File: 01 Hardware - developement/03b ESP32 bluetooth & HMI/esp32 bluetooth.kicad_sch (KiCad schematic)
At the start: 48 parts, among them J1 I2C, J2 UART, J3 power supply, J4 Jtag, J5 I2S, J8 Conn_01x01_Pin, SW10 Strapping button, SW8 Strapping button, SW9 Strapping button, U2 ESP32-DevKitC, U3 MCP23008

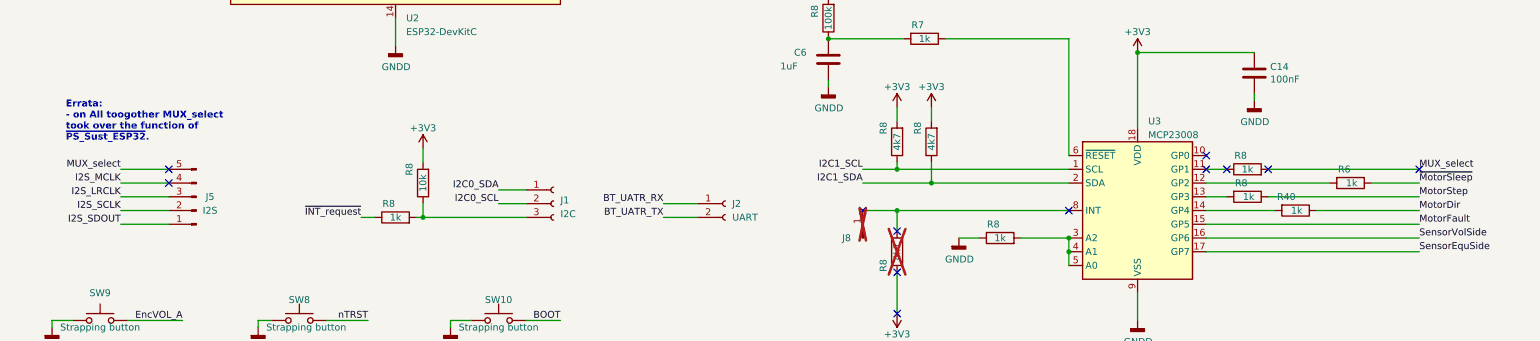
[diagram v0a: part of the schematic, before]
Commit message: hw and esp32 fw inprovements GOLDEN SAMPLE, restore point
- hw - poprawiono footprinty modułów i zamieniono mux select na power supply sustain pin
- fw - poprawiono kalsę StepperOptoPowerOFF
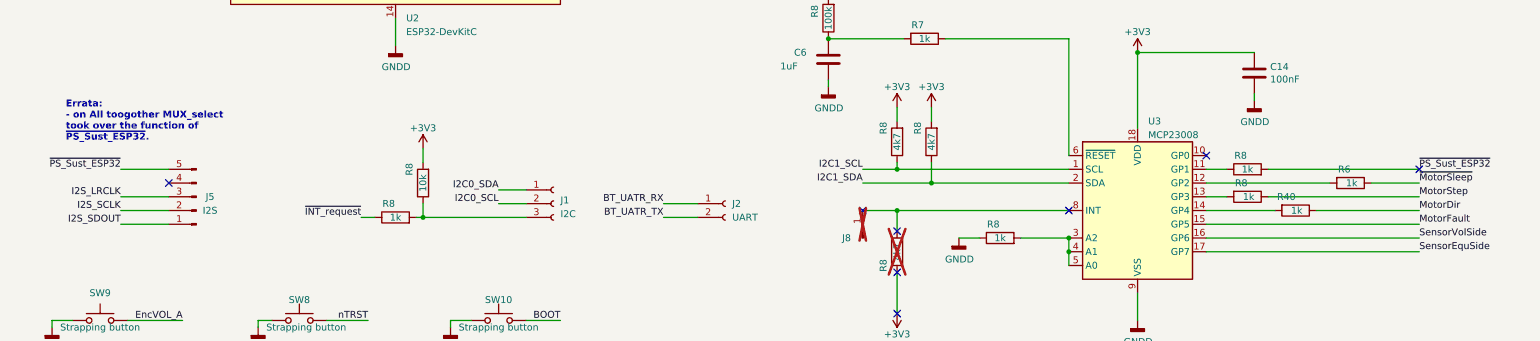
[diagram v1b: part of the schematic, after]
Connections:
- net I2S_MCLK: no longer names the net of J5.4 (Pin_4)
- net MUX_select renamed ~{PS_Sust_ESP32}
- no-connect marks 21 -> 17
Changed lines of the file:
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@@
   (no_connect (at 38.1 128.27))
   (no_connect (at 113.03 82.55))
-  (no_connect (at 233.68 125.73))
   (no_connect (at 113.03 85.09))
   (no_connect (at 113.03 80.01))
   (no_connect (at 68.58 177.8))
   (no_connect (at 113.03 87.63))
-  (no_connect (at 38.1 125.73))
   (no_connect (at 172.72 137.16))
-  (no_connect (at 229.87 125.73))
   (no_connect (at 269.24 125.73))
   (no_connect (at 166.37 133.35))
   (no_connect (at 172.72 152.4))
   (no_connect (at 204.47 133.35))
-  (no_connect (at 241.3 125.73))
   (no_connect (at 68.58 172.72))
   (no_connect (at 229.87 123.19))
@@
     (stroke (width 0) (type default))
   )
-  (wire (pts (xy 38.1 128.27) (xy 29.21 128.27))
-    (stroke (width 0) (type default))
-  )
   (wire (pts (xy 54.61 153.67) (xy 57.15 153.67))
     (stroke (width 0) (type default))
@@
     (effects (font (size 1.27 1.27)) (justify right bottom))
   )
-  (label "MUX_select" (at 269.24 125.73 0) (fields_autoplaced)
+  (label "~{PS_Sust_ESP32}" (at 269.24 125.73 0) (fields_autoplaced)
     (effects (font (size 1.27 1.27)) (justify left bottom))
   )
@@
     (effects (font (size 1.27 1.27)) (justify right bottom))
   )
-  (label "MUX_select" (at 29.21 125.73 180) (fields_autoplaced)
+  (label "~{PS_Sust_ESP32}" (at 29.21 125.73 180) (fields_autoplaced)
     (effects (font (size 1.27 1.27)) (justify right bottom))
   )
@@
     (effects (font (size 1.27 1.27)) (justify right bottom))
   )
-  (label "I2S_MCLK" (at 29.21 128.27 180) (fields_autoplaced)
-    (effects (font (size 1.27 1.27)) (justify right bottom))
-  )

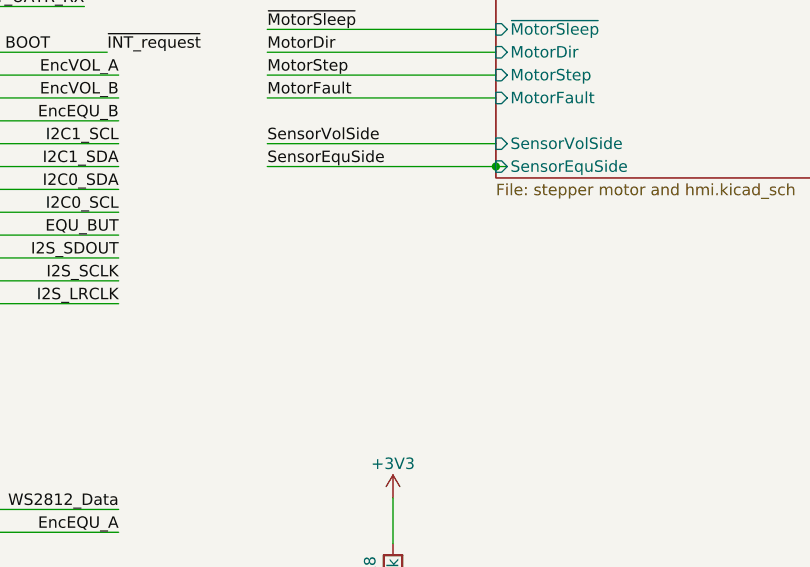
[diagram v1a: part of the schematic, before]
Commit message: stm32 -hw- pull-up resistors 10k
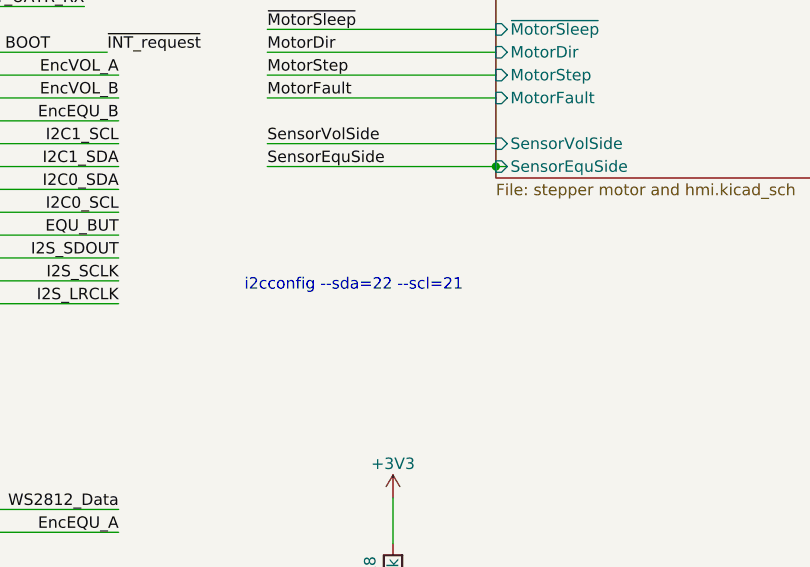
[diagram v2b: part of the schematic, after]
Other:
- note added: "i2cconfig --sda=22 --scl=21"
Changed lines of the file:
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@@
     )
+  )
+  (text "i2cconfig --sda=22 --scl=21" (at 143.51 66.04 0)
+    (effects (font (size 1.27 1.27)) (justify left bottom))
   )
   (text "Errata:\n- on All toogother MUX_select\ntook over the function of\n~{PS_Sust_ESP32}."

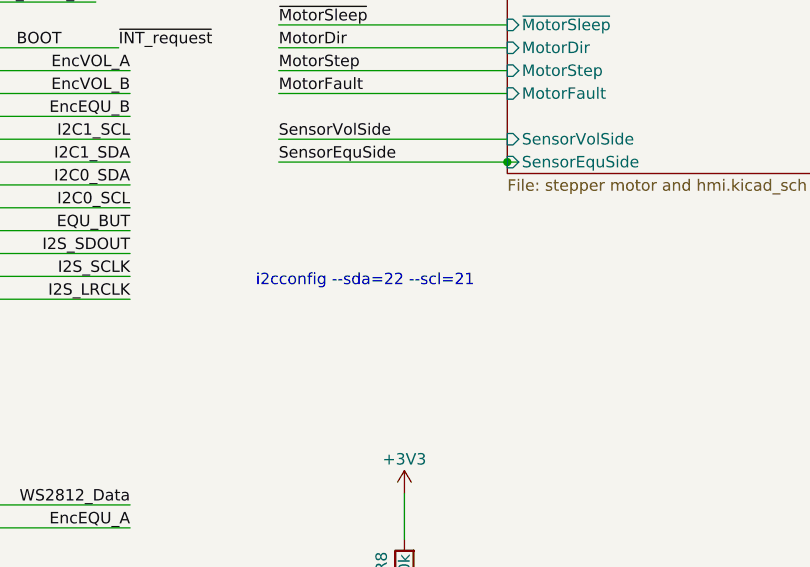
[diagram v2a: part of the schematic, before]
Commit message: i2c slave - coś zaczyna działać
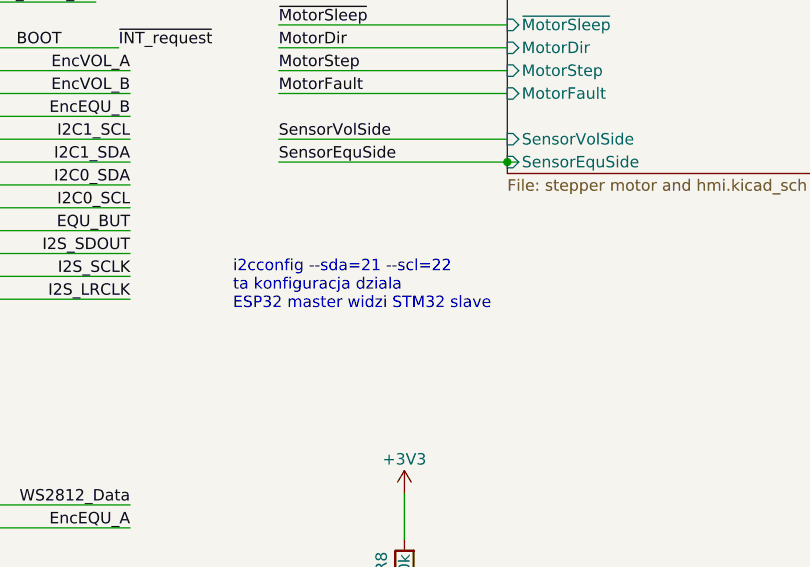
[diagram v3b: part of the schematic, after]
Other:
- note added: "i2cconfig --sda=21 --scl=22 ta konfiguracja dziala ESP32 master widzi STM32 slave"
- note removed: "i2cconfig --sda=22 --scl=21"
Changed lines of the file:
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@@
     )
   )
-  (text "i2cconfig --sda=22 --scl=21" (at 143.51 66.04 0)
+  (text "i2cconfig --sda=21 --scl=22\nta konfiguracja dziala\nESP32 master widzi STM32 slave"
+    (at 140.97 68.58 0)
     (effects (font (size 1.27 1.27)) (justify left bottom))
   )

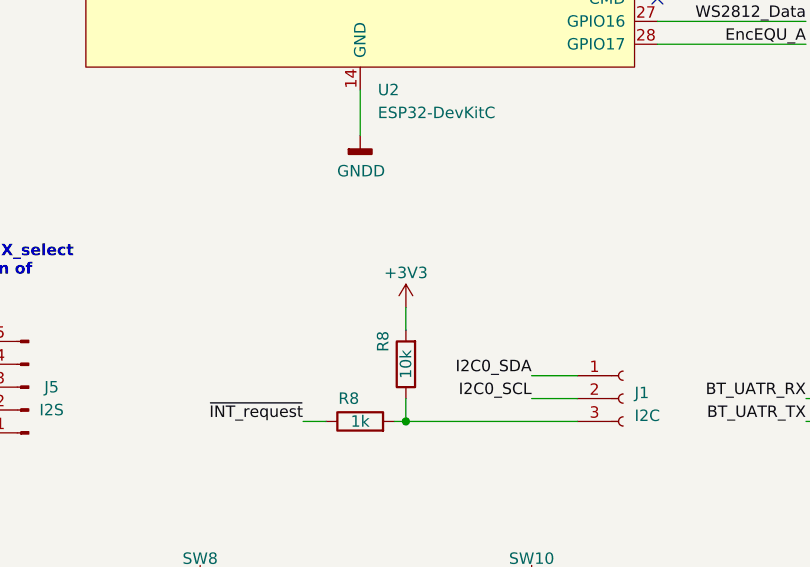
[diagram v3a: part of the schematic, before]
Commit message: ESP32 bluetooth & HMI -HW- interrupt request pull-down
Zmieniono R57 - pierwotnie rezystor ten był PULL-UP na linii i2cItterrupt request teraz jest PULL-DOWN
Zmiana jest po to, aby wykryć start ESp32. Po zboot'owaniu się ESP32 gaje sygnał na tej linii UP
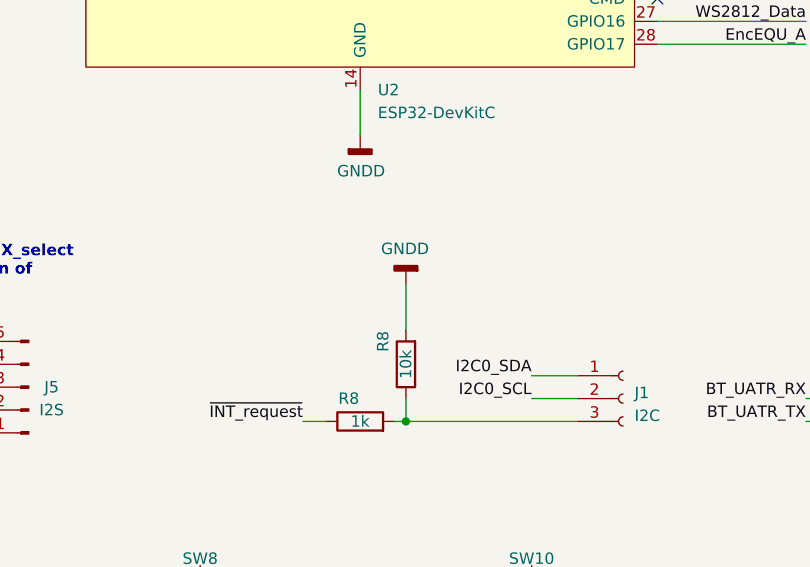
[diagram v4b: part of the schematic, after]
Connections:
- net +3V3: no longer R8.2
- net GNDD: now also R8.2
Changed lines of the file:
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@@
     (stroke (width 0) (type default))
   )
+  (wire (pts (xy 85.09 119.38) (xy 85.09 124.46))
+    (stroke (width 0) (type default))
+  )
   (wire (pts (xy 146.05 41.91) (xy 171.45 41.91))
     (stroke (width 0) (type default))
@@
     (stroke (width 0) (type default))
   )
-  (wire (pts (xy 85.09 121.92) (xy 85.09 124.46))
-    (stroke (width 0) (type default))
-  )
   (wire (pts (xy 223.52 44.45) (xy 240.03 44.45))
     (stroke (width 0) (type default))
@@
     )
   )
+  (symbol (lib_id "power:GNDD") (at 85.09 119.38 180) (unit 1)
+    (in_bom yes) (on_board yes) (dnp no)
+    (property "Reference" "#PWR071" (at 85.09 113.03 0)
+      (effects (font (size 1.27 1.27)) hide)
+    )
+    (property "Value" "GNDD" (at 84.9884 115.443 0)
+      (effects (font (size 1.27 1.27)))
+    )
+    (property "Footprint" "" (at 85.09 119.38 0)
+      (effects (font (size 1.27 1.27)) hide)
+    )
+    (property "Datasheet" "" (at 85.09 119.38 0)
+      (effects (font (size 1.27 1.27)) hide)
+    )
+    (pin "1")
+    (instances
+      (project "esp32 bluetooth"
+        (path "/85fd60db-6313-4d29-84e5-9ad356eb710e"
+          (reference "#PWR071") (unit 1)
+        )
+      )
+    )
+  )
   (symbol (lib_id "Device:C") (at 238.76 107.95 0) (unit 1)
     (in_bom yes) (on_board yes) (dnp no)
@@
         )
       )
-    )
-  )
-  (symbol (lib_id "power:+3V3") (at 85.09 121.92 0) (unit 1)
-    (in_bom yes) (on_board yes) (dnp no) (fields_autoplaced)
-    (property "Reference" "#PWR071" (at 85.09 125.73 0)
-      (effects (font (size 1.27 1.27)) hide)
-    )
-    (property "Value" "+3V3" (at 85.09 118.11 0)
-      (effects (font (size 1.27 1.27)))
-    )
-    (property "Footprint" "" (at 85.09 121.92 0)
-      (effects (font (size 1.27 1.27)) hide)
-    )
-    (property "Datasheet" "" (at 85.09 121.92 0)
-      (effects (font (size 1.27 1.27)) hide)
-    )
-    (pin "1")
-    (instances
-      (project "esp32 bluetooth"
-        (path "/85fd60db-6313-4d29-84e5-9ad356eb710e"
-          (reference "#PWR071") (unit 1)
-        )
-      )

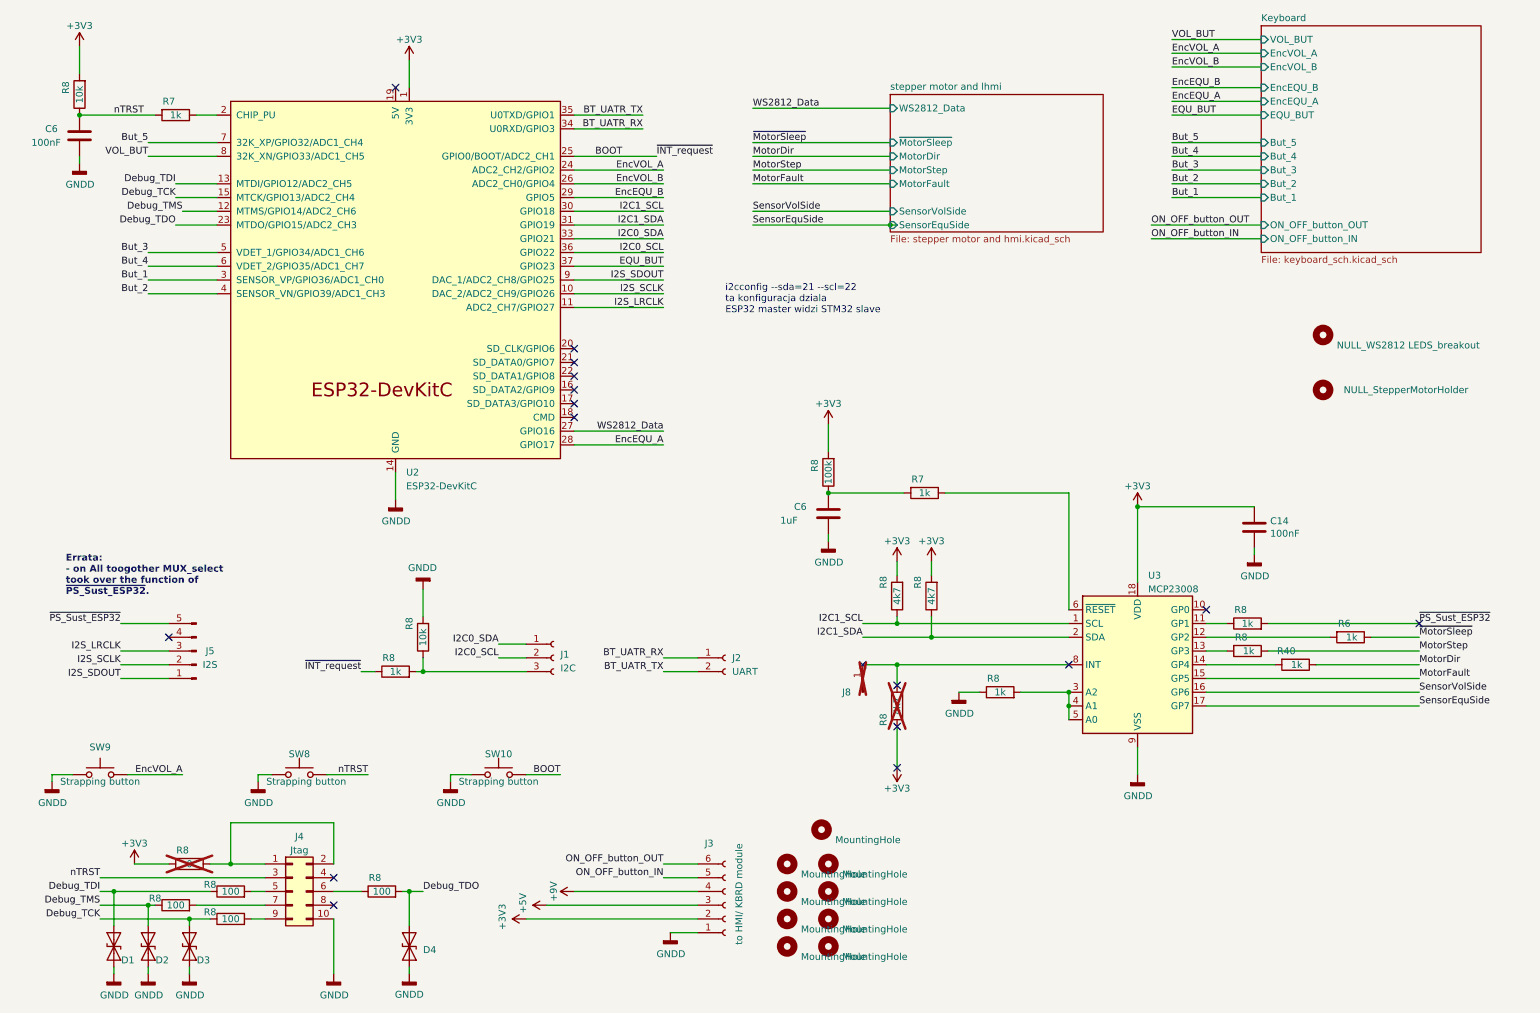
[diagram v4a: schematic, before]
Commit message: errata dot. rezystora R57 i bootowania
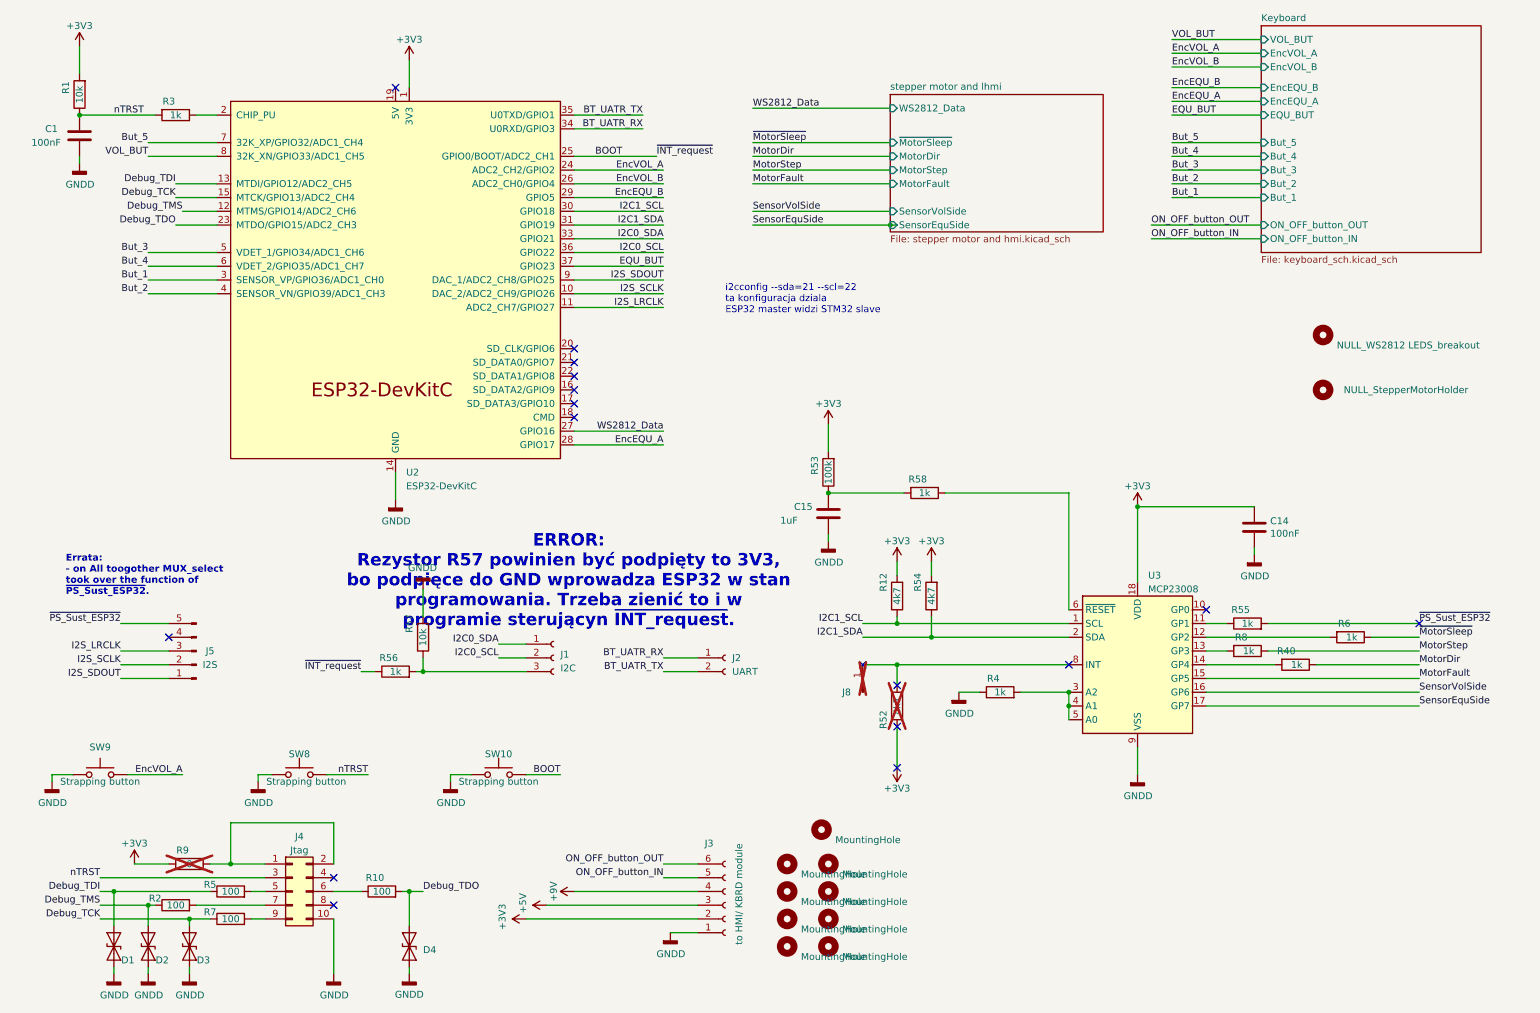
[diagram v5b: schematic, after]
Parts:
- renumbered C6 to C1, C6 to C15, R8 to R1, R8 to R10, R8 to R12, R8 to R2, R7 to R3, R8 to R4, R8 to R5, R8 to R52, R8 to R53, R8 to R54, R8 to R55, R8 to R56, R8 to R57, R7 to R58, R8 to R7, R8 to R9
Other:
- note added: "ERROR: Rezystor R57 powinien być podpięty to 3V3, bo podpięce do GND wprowadza ESP32 w stan programowania. Trzeba zienić to i w programie sterującyn ~{INT_request}."
